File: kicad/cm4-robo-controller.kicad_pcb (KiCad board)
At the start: 4 copper layers, 150 x 90 mm, 254 parts, among them CN1 SMA-KWE_C7498154, J1 KF7620-7.62-2P, J10 KF2EDGR-2.54-2P, J11 KF7620-7.62-2P, J12 KF2EDGR-2.54-2P, J13 KF2EDGR-2.54-2P, J14 KF7620-7.62-2P, J15 PM254-2-12-Z-8.5, J16 PM254-2-09-Z-8.5, J2 HX PZ2.54-2X5P TP, J3 Header-Male-2.54_2x3, J4 2541WV-2X12P, J5 Header-Male-2.54_1x3, J6 Header-Male-2.54_2x3, J7 SMA-KWE_C7498154, J8 KF2EDGR-2.54-4P, J9 KF2EDGR-2.54-3P, Q1 SP40P04NK, Q2 DMP6023LE-13, Q3 NCE6008AS, Q4 BSS138, SW1 SS-12F49-G050, U1 74LVC1G07SE-7, U10 74LVC1G07SE-7, U11 MX26631DL, U12 MAX-M10S-00B, U13 74LVC1G17SE-7, U14 74LVC1G17SE-7, U15 AP64501SP-13, U16 74LVC1G17SE-7, U17 74LVC1G07SE-7, U18 TPS70933DBVR, U19 74LVC1G17SE-7, U2 FSUSB42MUX, U3 USB2514B-I/M2, U4 AP22653W6-7, U5 TPD4EUSB30DQAR, U6 TPD4EUSB30DQAR, U7 TPD4EUSB30DQAR, U8 TPD4EUSB30DQAR, U9 TPD4EUSB30DQAR, X1 24MHz

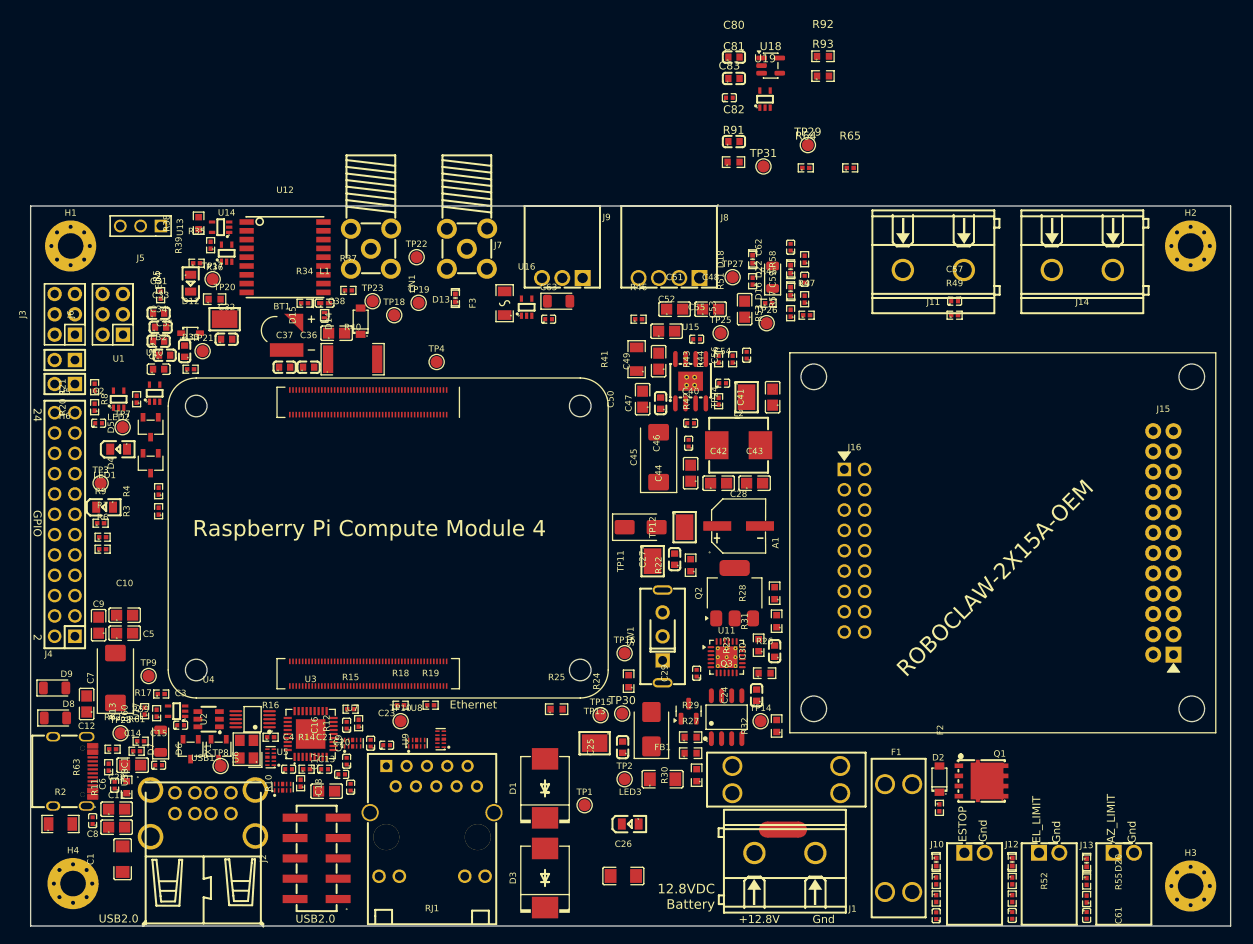
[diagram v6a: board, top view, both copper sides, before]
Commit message: PCB placement and routing snapshot before layout rework
Power, battery-input, Power_5V (AP64501 per datasheet Figure 31) and Robo
sheets placed and routed; CHASSIS bonding for H1-H4; board outline at
60-210 x 49.6-139.6.

Footprint fixes: U11 thermal vias 0.3 mm drill; U15 exposed-pad holes
numbered as pad 9 (GND). Net classes for high-current nets.
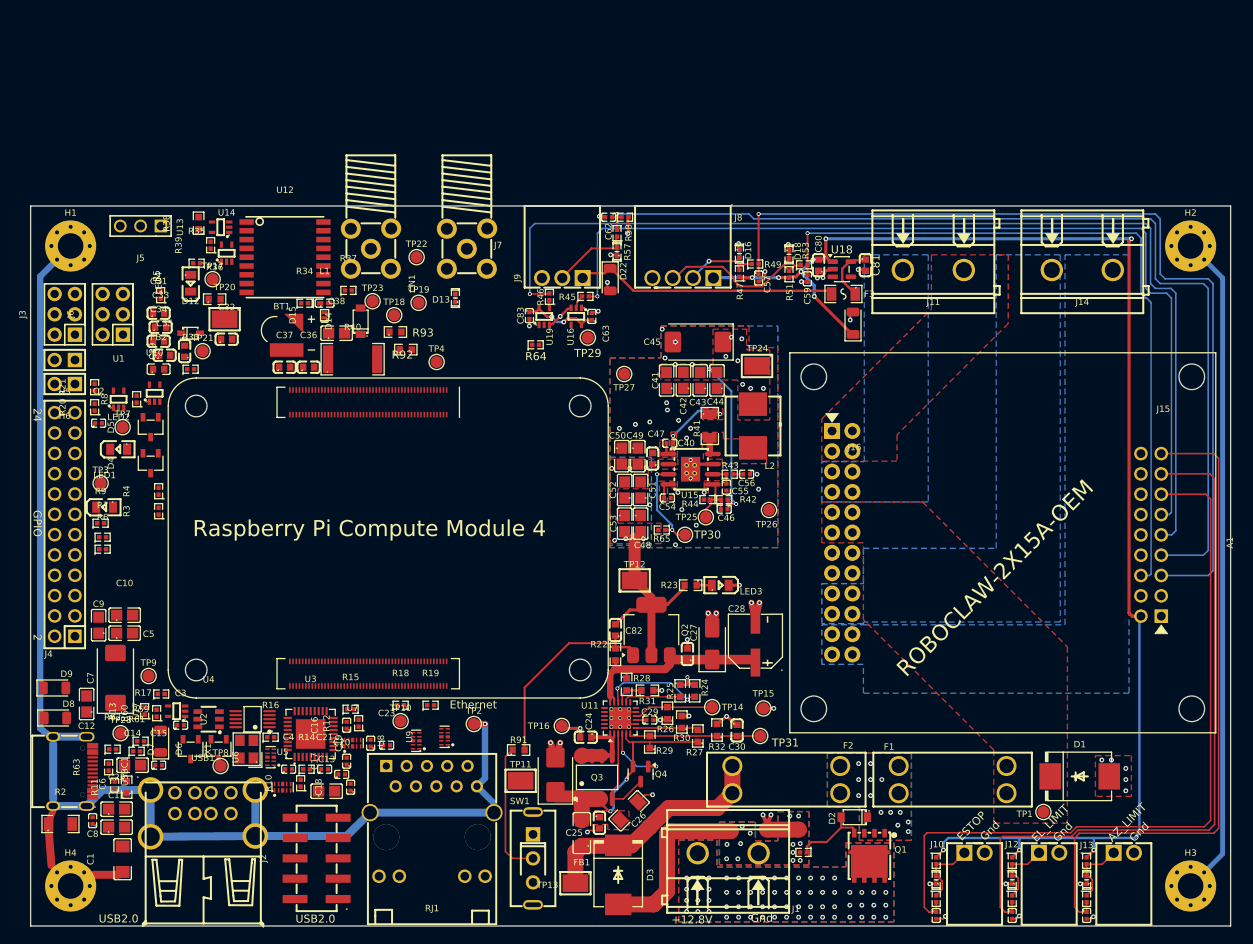
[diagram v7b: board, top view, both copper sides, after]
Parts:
- moved R91 78.2 mm to (121.0, 117.6)
- moved TP31 71.2 mm to (151.2, 115.8)
- moved D1 66.9 mm to (191.1, 120.9), turned to 0 degrees
- moved R92 63.7 mm to (106.9, 67.5)
- moved C82 62.8 mm to (133.1, 102.6), turned to 90 degrees
- moved R93 62.3 mm to (105.6, 65.3)
- moved TP1 57.4 mm to (186.6, 125.3)
- moved R65 51.0 mm to (138.9, 90.1), turned to 180 degrees
- moved F3 42.4 mm to (161.6, 60.6), turned to 180 degrees
- moved R64 40.4 mm to (123.1, 67.0)
- moved U19 38.7 mm to (124.2, 63.4)
- moved C83 37.0 mm to (122.3, 63.3), turned to -90 degrees
- moved TP29 36.5 mm to (129.7, 66.0)
- moved SW1 32.1 mm to (122.8, 131.2), turned to -90 degrees
- moved TP11 32.0 mm to (121.2, 121.5), turned to 180 degrees
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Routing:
- net CHASSIS: track 0.00 -> 240.7 mm, vias 0 -> 1
- net /Robo/RC_5V: track 0.00 -> 174.4 mm, vias 0 -> 10
- net Net-(A1-S1_RX): track 0.00 -> 130.4 mm, vias 0 -> 1
- net /Robo/EN2_A: track 0.00 -> 123.2 mm, vias 0 -> 1
- net Net-(A1-S2_TX): track 0.00 -> 116.1 mm, vias 0 -> 1
- net /Robo/EN1_A: track 0.00 -> 114.0 mm, vias 0 -> 1
- net /Robo/ESTOP: track 0.00 -> 95.1 mm
- net /Robo/EN1_B: track 0.00 -> 90.3 mm, vias 0 -> 1
- net /Robo/EL_LIMIT: track 0.00 -> 89.2 mm
- net /Robo/AZ_LIMIT: track 0.00 -> 83.8 mm
- net GND: track 0.00 -> 40.4 mm, vias 0 -> 42
- net PGND: track 0.00 -> 39.1 mm, vias 0 -> 36
- net /Robo/AZ_ENC_3V3: track 0.00 -> 30.8 mm
- net /battery-input/V_BAT: track 0.00 -> 29.9 mm
- net /power/V_BAT_F: track 0.00 -> 29.7 mm, vias 0 -> 2
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- added copper zone on F.Cu, net /5V
- added copper zone on F.Cu, net /Robo/M1A
- added copper zone on B.Cu, net /Robo/M1B
- added copper zone on B.Cu, net /Robo/M2A
- added copper zone on B.Cu, net /Robo/M2B
- added copper zone on F.Cu, net /Robo/V_MOTOR
- added copper zone on B.Cu, net /power/12V
- added copper zone on F.Cu, net /power/12V
- added copper zone on F.Cu, net /power/V_BAT_F
- added copper zone on B.Cu, net GND
- added copper zone on F.Cu, net GND
- added copper zone on F.Cu, net Net-(C40-Pad1)
- added copper zone on B.Cu, net Net-(D2-K)
- added copper zone on F.Cu, net Net-(D2-K)
- added copper zone on B.Cu, net Net-(J1-Pad1)
- added copper zone on F.Cu, net Net-(J1-Pad1)
- added copper zone on F.Cu, net Net-(U15-BST)
- added copper zone on F.Cu, net Net-(U15-FB)
- added copper zone on F.Cu, net Net-(U15-SS)
- added copper zone on F.Cu, net Net-(U15-SW)
- added copper zone on B.Cu, net PGND
- added copper zone on F.Cu, net PGND
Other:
- board text removed: "12.8VDC Battery"
